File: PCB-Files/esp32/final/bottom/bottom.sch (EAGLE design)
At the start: 41 parts, among them X2 ESP32_WROOM32_SKINNY

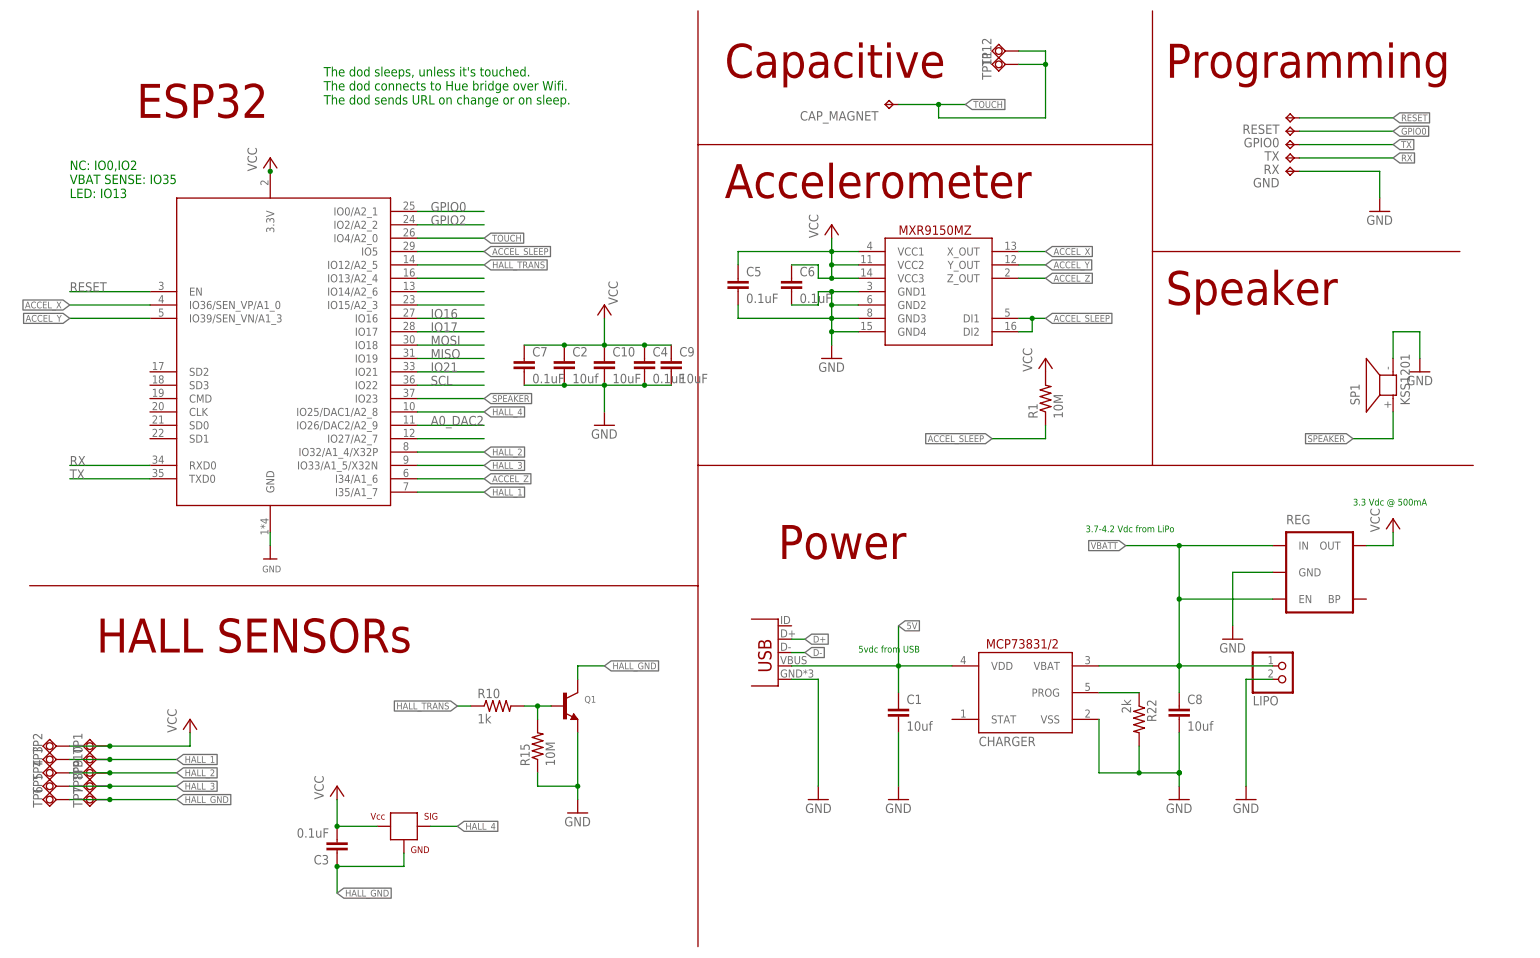
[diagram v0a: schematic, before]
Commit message: creates final PCB version; revised beta side pcbs to match beta main pcb pinouts
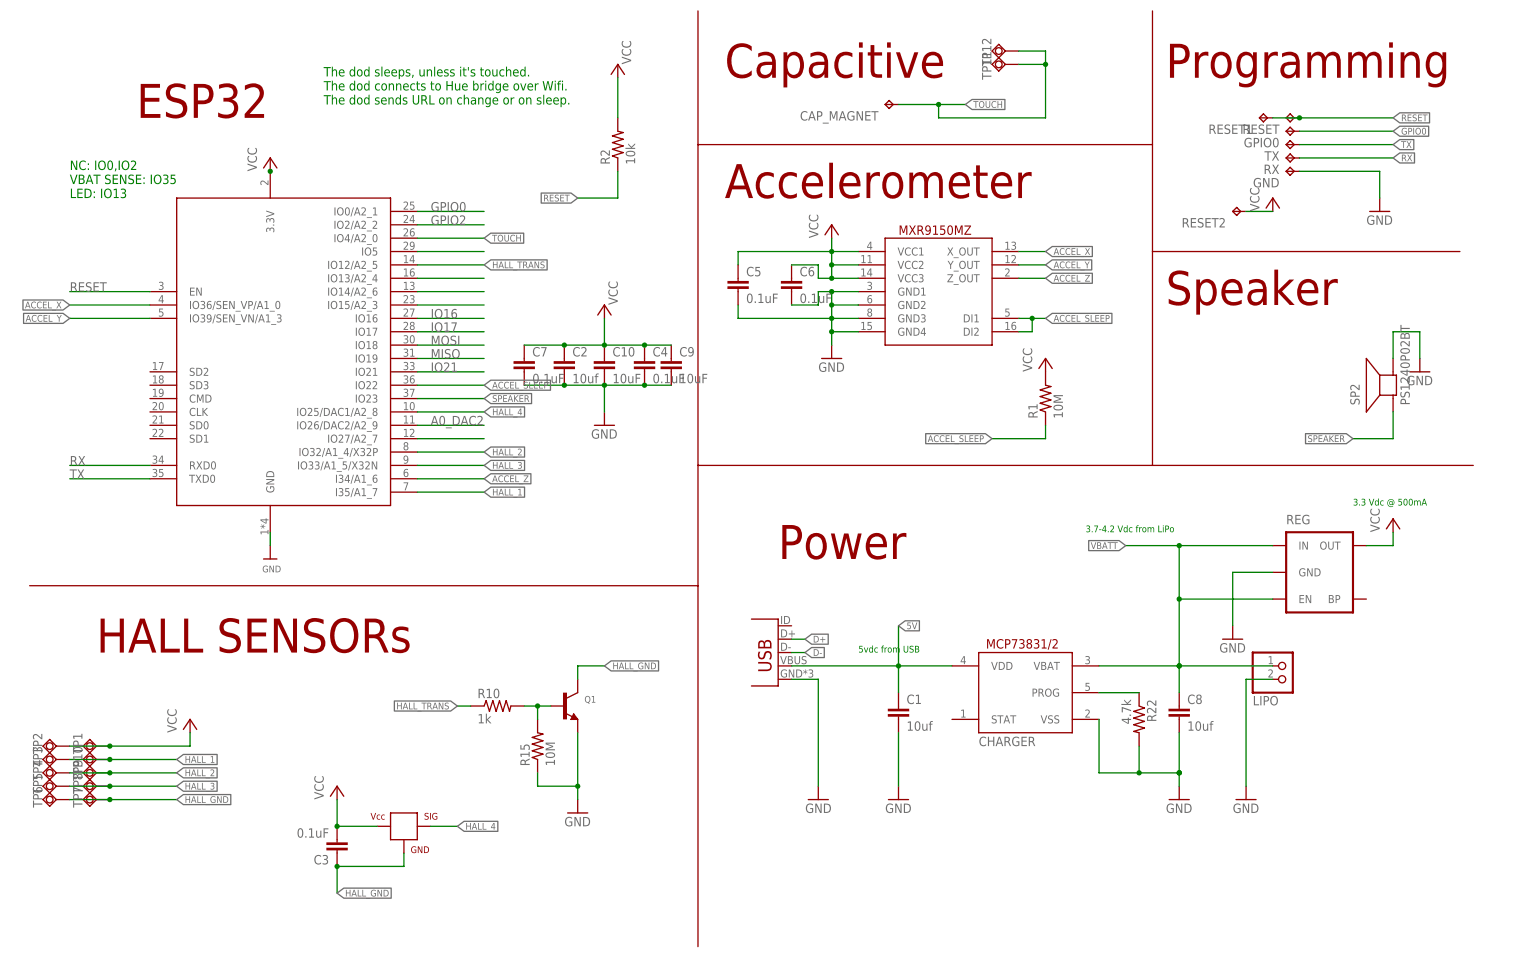
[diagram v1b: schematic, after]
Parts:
- removed SP1: KSS1201, buzzer:KSS1201
- added R2: 10k, SparkFun-Passives:RESISTOR0402-RES
- added RESET1, RESET2: TPTP13R, testpad:TPTP13R
- added SP2: PS1240P02BT, adafruit:SPEAKER/PS12
- R22: value 2k -> 4.7k
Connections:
- removed net SCL: X2.IO22
- new net N$3: X2.IO5
- net ACCEL_SLEEP: now also X2.IO22; no longer X2.IO5
- net GND: now also SP2.-; no longer SP1.2
- net RESET: now also R2.1, RESET1.TP
- net SPEAKER: now also SP2.+; no longer SP1.1
- net VCC: now also R2.2, RESET2.TP
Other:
- note added: "SCL"
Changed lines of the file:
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@@
 <part name="P+7" library="supply1" library_urn="urn:adsk.eagle:library:371" deviceset="VCC" device=""/>
 <part name="GND15" library="supply1" library_urn="urn:adsk.eagle:library:371" deviceset="GND" device=""/>
-<part name="R22" library="SparkFun-Passives" deviceset="RESISTOR" device="0402-RES" value="2k"/>
+<part name="R22" library="SparkFun-Passives" deviceset="RESISTOR" device="0402-RES" value="4.7k"/>
 <part name="C10" library="SparkFun" deviceset="CAP" device="0402-CAP" value="10uF"/>
 <part name="R10" library="SparkFun-Passives" deviceset="RESISTOR" device="0402-RES" value="1k"/>
@@
 <part name="C5" library="SparkFun" deviceset="CAP" device="0402-CAP" value="0.1uF"/>
 <part name="C6" library="SparkFun" deviceset="CAP" device="0402-CAP" value="0.1uF"/>
-<part name="SP1" library="buzzer" library_urn="urn:adsk.eagle:library:113" deviceset="KSS1201" device="" package3d_urn="urn:adsk.eagle:package:5268/1"/>
 <part name="RESET" library="testpad" library_urn="urn:adsk.eagle:library:385" deviceset="TP" device="TP13R" package3d_urn="urn:adsk.eagle:package:27967/1"/>
 <part name="GPIO0" library="testpad" library_urn="urn:adsk.eagle:library:385" deviceset="TP" device="TP13R" package3d_urn="urn:adsk.eagle:package:27967/1"/>
@@
 <part name="C7" library="SparkFun" deviceset="CAP" device="0402-CAP" value="0.1uF"/>
 <part name="C9" library="SparkFun" deviceset="CAP" device="0402-CAP" value="10uF"/>
+<part name="R2" library="SparkFun-Passives" deviceset="RESISTOR" device="0402-RES" value="10k"/>
+<part name="P+6" library="supply1" library_urn="urn:adsk.eagle:library:371" deviceset="VCC" device=""/>
+<part name="SP2" library="adafruit" library_urn="urn:adsk.eagle:library:420" deviceset="SPEAKER" device="/PS12" package3d_urn="urn:adsk.eagle:package:6240663/1" value="PS1240P02BT"/>
+<part name="RESET1" library="testpad" library_urn="urn:adsk.eagle:library:385" deviceset="TP" device="TP13R" package3d_urn="urn:adsk.eagle:package:27967/1"/>
+<part name="RESET2" library="testpad" library_urn="urn:adsk.eagle:library:385" deviceset="TP" device="TP13R" package3d_urn="urn:adsk.eagle:package:27967/1"/>
+<part name="P+8" library="supply1" library_urn="urn:adsk.eagle:library:371" deviceset="VCC" device=""/>
 </parts>
 <sheets>
@@
 <text x="76.2" y="134.62" size="1.778" layer="150">SCK/IO5</text>
 <text x="76.2" y="106.68" size="1.778" layer="150">SDA/IO23</text>
+<text x="76.2" y="109.22" size="1.778" layer="150">SCL</text>
 </plain>
 <instances>
@@
 <attribute name="VALUE" x="146.304" y="124.841" size="1.778" layer="96"/>
 </instance>
-<instance part="SP1" gate="1" x="259.08" y="109.22" smashed="yes" rot="R90">
-<attribute name="NAME" x="252.73" y="105.41" size="1.778" layer="95" rot="R90"/>
-<attribute name="VALUE" x="262.255" y="105.41" size="1.778" layer="96" rot="R90"/>
-</instance>
 <instance part="RESET" gate="G$1" x="238.76" y="160.02" smashed="yes" rot="R90">
 <attribute name="NAME" x="237.49" y="158.75" size="1.778" layer="95" rot="R180"/>
@@
 <attribute name="NAME" x="123.444" y="114.681" size="1.778" layer="95"/>
 <attribute name="VALUE" x="123.444" y="109.601" size="1.778" layer="96"/>
+</instance>
+<instance part="R2" gate="G$1" x="111.76" y="154.94" smashed="yes" rot="R90">
+<attribute name="NAME" x="110.2614" y="151.13" size="1.778" layer="95" rot="R90"/>
+<attribute name="VALUE" x="115.062" y="151.13" size="1.778" layer="96" rot="R90"/>
+</instance>
+<instance part="P+6" gate="VCC" x="111.76" y="170.18" smashed="yes">
+<attribute name="VALUE" x="114.3" y="170.18" size="1.778" layer="96" rot="R90"/>
+</instance>
+<instance part="SP2" gate="S1" x="259.08" y="109.22" smashed="yes" rot="R90">
+<attribute name="NAME" x="252.73" y="105.41" size="1.778" layer="95" rot="R90"/>
+<attribute name="VALUE" x="262.255" y="105.41" size="1.778" layer="96" rot="R90"/>
+</instance>
+<instance part="RESET1" gate="G$1" x="233.68" y="160.02" smashed="yes" rot="R90">
+<attribute name="NAME" x="232.41" y="158.75" size="1.778" layer="95" rot="R180"/>
+<attribute name="TP_SIGNAL_NAME" x="234.95" y="161.29" size="1.778" layer="97" rot="R90"/>
+</instance>
+<instance part="RESET2" gate="G$1" x="228.6" y="142.24" smashed="yes" rot="R90">
+<attribute name="NAME" x="227.33" y="140.97" size="1.778" layer="95" rot="R180"/>
+<attribute name="TP_SIGNAL_NAME" x="229.87" y="143.51" size="1.778" layer="97" rot="R90"/>
+</instance>
+<instance part="P+8" gate="VCC" x="236.22" y="144.78" smashed="yes">
+<attribute name="VALUE" x="233.68" y="142.24" size="1.778" layer="96" rot="R90"/>
 </instance>
 </instances>
@@
 </segment>
 <segment>
-<pinref part="SP1" gate="1" pin="2"/>
 <wire x1="259.08" y1="114.3" x2="259.08" y2="119.38" width="0.1524" layer="91"/>
 <wire x1="259.08" y1="119.38" x2="264.16" y2="119.38" width="0.1524" layer="91"/>
 <wire x1="264.16" y1="119.38" x2="264.16" y2="114.3" width="0.1524" layer="91"/>
 <pinref part="GND7" gate="1" pin="GND"/>
+<pinref part="SP2" gate="S1" pin="-"/>
 </segment>
 </net>
@@
 <pinref part="P+3" gate="VCC" pin="VCC"/>
 </segment>
+<segment>
+<pinref part="R2" gate="G$1" pin="2"/>
+<wire x1="111.76" y1="160.02" x2="111.76" y2="167.64" width="0.1524" layer="91"/>
+<pinref part="P+6" gate="VCC" pin="VCC"/>
+</segment>
+<segment>
+<pinref part="RESET2" gate="G$1" pin="TP"/>
+<wire x1="231.14" y1="142.24" x2="236.22" y2="142.24" width="0.1524" layer="91"/>
+<pinref part="P+8" gate="VCC" pin="VCC"/>
+</segment>
 </net>
 <net name="HALL_1" class="0">
@@
 <label x="259.08" y="160.02" size="1.27" layer="95" xref="yes"/>
 <pinref part="RESET" gate="G$1" pin="TP"/>
+<pinref part="RESET1" gate="G$1" pin="TP"/>
+<wire x1="241.3" y1="160.02" x2="236.22" y2="160.02" width="0.1524" layer="91"/>
+<junction x="241.3" y="160.02"/>
+</segment>
+<segment>
+<pinref part="R2" gate="G$1" pin="1"/>
+<wire x1="111.76" y1="149.86" x2="111.76" y2="144.78" width="0.1524" layer="91"/>
+<wire x1="111.76" y1="144.78" x2="104.14" y2="144.78" width="0.1524" layer="91"/>
+<label x="104.14" y="144.78" size="1.27" layer="95" rot="R180" xref="yes"/>
 </segment>
 </net>
@@
 <label x="76.2" y="116.84" size="1.778" layer="150"/>
 <pinref part="X2" gate="G$1" pin="IO18"/>
-</segment>
-</net>
-<net name="SCL" class="0">
-<segment>
-<wire x1="73.66" y1="109.22" x2="86.36" y2="109.22" width="0.1524" layer="91"/>
-<label x="76.2" y="109.22" size="1.778" layer="150"/>
-<pinref part="X2" gate="G$1" pin="IO22"/>
 </segment>
 </net>
@@
 </segment>
 <segment>
-<wire x1="73.66" y1="134.62" x2="86.36" y2="134.62" width="0.1524" layer="91"/>
-<pinref part="X2" gate="G$1" pin="IO5"/>
-<label x="86.36" y="134.62" size="1.27" layer="95" xref="yes"/>
-</segment>
-<segment>
 <pinref part="R1" gate="G$1" pin="1"/>
 <wire x1="193.04" y1="101.6" x2="193.04" y2="99.06" width="0.1524" layer="91"/>
 <wire x1="193.04" y1="99.06" x2="182.88" y2="99.06" width="0.1524" layer="91"/>
 <label x="182.88" y="99.06" size="1.27" layer="95" rot="R180" xref="yes"/>
+</segment>
+<segment>
+<pinref part="X2" gate="G$1" pin="IO22"/>
+<wire x1="73.66" y1="109.22" x2="86.36" y2="109.22" width="0.1524" layer="91"/>
+<label x="86.36" y="109.22" size="1.27" layer="95" xref="yes"/>
 </segment>
 </net>
@@
 </segment>
 <segment>
-<pinref part="SP1" gate="1" pin="1"/>
 <wire x1="259.08" y1="104.14" x2="259.08" y2="99.06" width="0.1524" layer="91"/>
 <wire x1="259.08" y1="99.06" x2="251.46" y2="99.06" width="0.1524" layer="91"/>
 <label x="251.46" y="99.06" size="1.27" layer="95" rot="R180" xref="yes"/>
-</segment>
-</net>
+<pinref part="SP2" gate="S1" pin="+"/>
+</segment>
+</net>
+<net name="N$3" class="0">
+<segment>
+<pinref part="X2" gate="G$1" pin="IO5"/>
+<wire x1="73.66" y1="134.62" x2="86.36" y2="134.62" width="0.1524" layer="91"/>
+</segment>
+</net>
